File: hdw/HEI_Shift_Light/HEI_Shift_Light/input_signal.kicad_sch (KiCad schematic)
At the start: 14 parts

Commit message: more schematic progress
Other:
- note added: "Unsure on if this is supposed to be resistor to GND or midrail"
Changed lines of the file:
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@@
+		)
+	)
+	(bezier
+		(pts
+			(xy 124.46 77.47) (xy 124.46 77.47) (xy 104.14 49.53) (xy 104.14 49.53)
+		)
+		(stroke
+			(width 0)
+			(type default)
+		)
+		(fill
+			(type none)
 		)
 	)
@@
 		(exclude_from_sim no)
 		(at 199.136 62.992 0)
+		(effects
+			(font
+				(size 1.27 1.27)
+			)
+		)
+	)
+	(text "Unsure on if this is supposed to\nbe resistor to GND or midrail"
+		(exclude_from_sim no)
+		(at 103.378 47.752 0)
 		(effects
 			(font
@@
 			(hide yes)
 			(show_name no)
+			(do_not_autoplace no)
+			(effects
+				(font
+					(size 1.27 1.27)
+				)
+				(justify left)
+			)
+		)
+	)
+	(global_label "TACH_PULSE"
+		(shape output)
+		(at 157.48 40.64 0)
+		(fields_autoplaced yes)
+		(effects
+			(font
+				(size 1.27 1.27)
+			)
+			(justify left)
+		)
+		(property "Intersheetrefs" "${INTERSHEET_REFS}"
+			(at 172.0766 40.64 0)
+			(hide yes)
+			(show_name no)

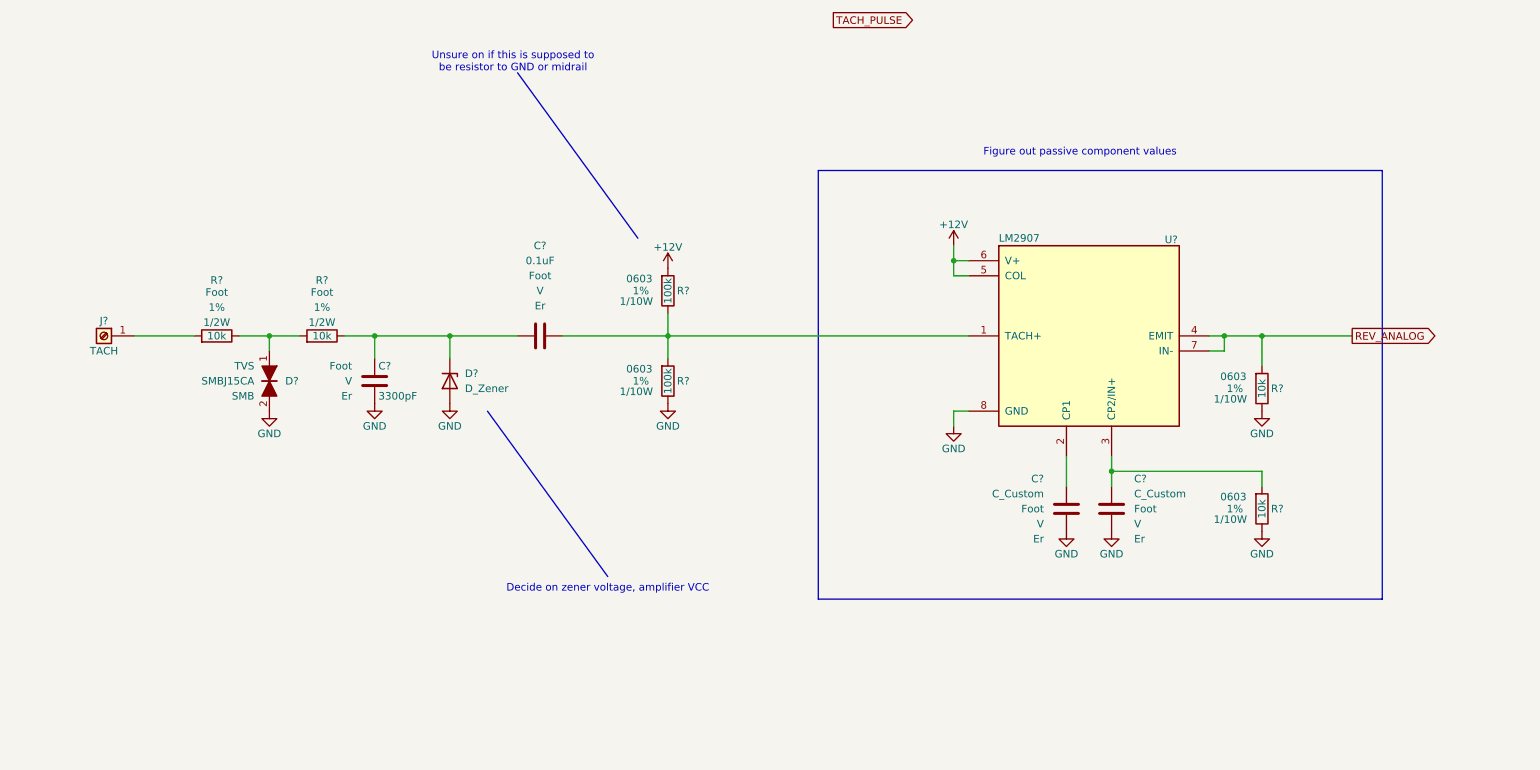
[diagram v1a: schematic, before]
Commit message: populated input protection circuit passive components, updated PIC pinout, added stuff to frequency to voltage converter circuit
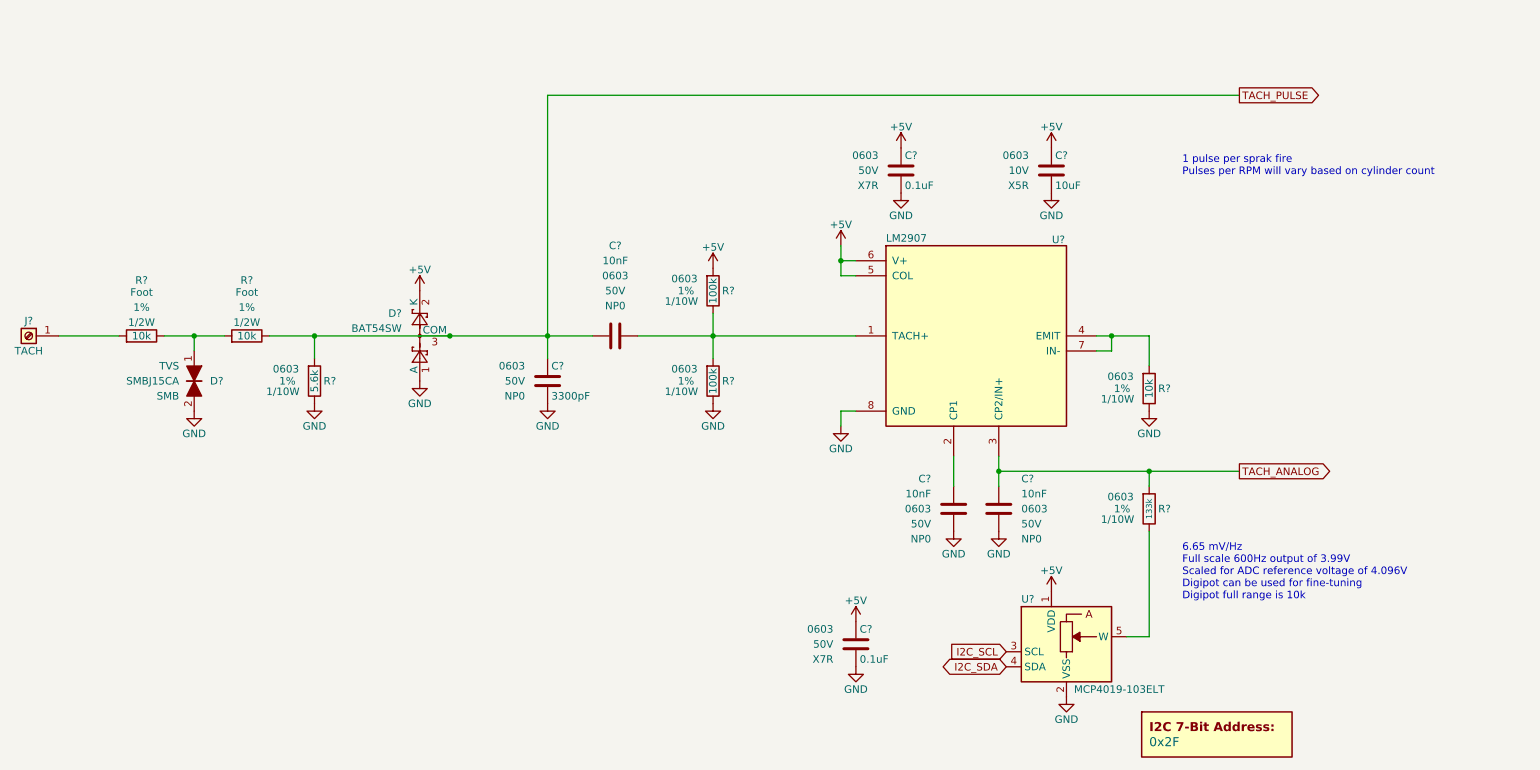
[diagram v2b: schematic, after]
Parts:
- removed C?: 0.1uF, symbol Custom Library:C_Custom
- removed C?: C_Custom, symbol Custom Library:C_Custom
- removed D?: D_Zener, symbol Device:D_Zener
- added C? (x2): 0.1uF, Capacitors_SMD:C_0603, symbol Custom_Library:C_Custom
- added C?: 10uF, Capacitors_SMD:C_0603, symbol Custom_Library:C_Custom
- added C? (x2): 10nF, symbol Custom Library:C_Custom
- added D?: BAT54SW, Package_TO_SOT_SMD:SOT-323_SC-70, symbol Diode:BAT54SW
- added DOC?: 0x2F, symbol Custom Library:I2C_Address
- added R?: 5.6k, Resistors_SMD:R_0603, symbol Custom_Library:R_Custom
- added U?: MCP4019-103ELT, Package_TO_SOT_SMD:SOT-353_SC-70-5, symbol Potentiometer_Digital:MCP4019-xxxxLT
- C?: Dielectric Er -> NP0; Voltage V -> 50V; display_footprint Foot -> 0603
- C?: value C_Custom -> 10nF; Dielectric Er -> NP0; Digi-Key PN PN -> 311-3960-1-ND; Voltage V -> 50V; display_footprint Foot -> 0603
- R?: value 10k -> 133k; Digi-Key PN 541-10.0KHCT-ND -> (none)
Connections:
- net GND: now also C?.2, C?.2, C?.2, C?.2, D?.1 (A), R?.2, U?.2 (VSS); no longer R?.2
- net TACH_PULSE: now also C?.1, R?.2, C?.1, D?.3 (COM), R?.1
- net TACH_ANALOG: now reaches R?.1, U?.3 (CP2/IN+)
- net TACH_ANALOG: now also C?.1
- net at R?.1, R?.2, U?.1 (TACH+): now also C?.2
- net +12V renamed +5V
- net +5V: now also C?.1, C?.1, C?.1, D?.2 (K), U?.1 (VDD)
- net REV_ANALOG: no longer names the net of R?.1, U?.4 (EMIT), U?.7 (IN-)
- new net: R?.2, U?.5 (W)
- new net I2C_SCL: U?.3 (SCL)
- new net I2C_SDA: U?.4 (SDA)
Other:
- note added: "1 pulse per sprak fire Pulses per RPM will vary based on cylinder count"
- note added: "6.65 mV/Hz Full scale 600Hz output of 3.99V Scaled for ADC reference voltage of 4.096V Digipot can be used for fine-tuning Digipot full range is 10k"
- note removed: "Decide on zener voltage, amplifier VCC"
- note removed: "Figure out passive component values"
- note removed: "Unsure on if this is supposed to be resistor to GND or midrail"
- moved on the sheet: C?, D?, J?, R?, U?

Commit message: added more shit, RGD LED, LC input filter
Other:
- note added: "1 pulse per spark fire Pulses per RPM will vary based on cylinder count"
- note removed: "1 pulse per sprak fire Pulses per RPM will vary based on cylinder count"
- company: (none) -> Drew Maatman
- title: (none) -> HEI Shift Light
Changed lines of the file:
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@@
 	(generator_version "10.0")
 	(paper "A")
+	(title_block
+		(title "HEI Shift Light")
+		(date "2026-05-29")
+		(rev "A")
+		(company "Drew Maatman")
+	)
 	(text "6.65 mV/Hz\nFull scale 600Hz output of 3.99V\nScaled for ADC reference voltage of 4.096V\nDigipot can be used for fine-tuning\nDigipot full range is 10k"
 		(exclude_from_sim no)
@@
 		)
 	)
-	(text "1 pulse per sprak fire\nPulses per RPM will vary based on cylinder count"
+	(text "1 pulse per spark fire\nPulses per RPM will vary based on cylinder count"
 		(exclude_from_sim no)
 		(at 216.408 65.278 0)
@@
 		(in_pos_files yes)
 		(dnp no)
-		(property "Reference" "#PWR044"
+		(property "Reference" "#PWR?"
 			(at 168.91 76.2 0)
 			(hide yes)
@@
 			(project "HEI_Shift_Light"
 				(path "/288c8230-69eb-4ad9-929d-f4630114196f/3f3e3aac-043b-4713-af21-26e9e85000ef"
-					(reference "#PWR044")
+					(reference "#PWR?")
 					(unit 1)
 				)
@@
 		(in_pos_files yes)
 		(dnp no)
-		(property "Reference" "#PWR03"
+		(property "Reference" "#PWR?"
 			(at 87.63 107.95 0)
 			(hide yes)
@@
 			(project "HEI_Shift_Light"
 				(path "/288c8230-69eb-4ad9-929d-f4630114196f/3f3e3aac-043b-4713-af21-26e9e85000ef"
-					(reference "#PWR03")
+					(reference "#PWR?")
 					(unit 1)
 				)
@@
 		(in_pos_files yes)
 		(dnp no)
-		(property "Reference" "#PWR05"
+		(property "Reference" "#PWR?"
 			(at 194.31 140.97 0)
 			(hide yes)
@@
 			(project "HEI_Shift_Light"
 				(path "/288c8230-69eb-4ad9-929d-f4630114196f/3f3e3aac-043b-4713-af21-26e9e85000ef"
-					(reference "#PWR05")
+					(reference "#PWR?")
 					(unit 1)
 				)
@@
 		(in_pos_files yes)
 		(dnp no)
-		(property "Reference" "#PWR01"
+		(property "Reference" "#PWR?"
 			(at 158.75 82.55 0)
 			(hide yes)
@@
 			(project "HEI_Shift_Light"
 				(path "/288c8230-69eb-4ad9-929d-f4630114196f/3f3e3aac-043b-4713-af21-26e9e85000ef"
-					(reference "#PWR01")
+					(reference "#PWR?")
 					(unit 1)
 				)
@@
 		(in_pos_files yes)
 		(dnp no)
-		(property "Reference" "#PWR038"
+		(property "Reference" "#PWR?"
 			(at 196.85 161.29 0)
 			(hide yes)
@@
 			(project "HEI_Shift_Light"
 				(path "/288c8230-69eb-4ad9-929d-f4630114196f/3f3e3aac-043b-4713-af21-26e9e85000ef"
-					(reference "#PWR038")
+					(reference "#PWR?")
 					(unit 1)
 				)
@@
 		(in_pos_files yes)
 		(dnp no)
-		(property "Reference" "#PWR039"
+		(property "Reference" "#PWR?"
 			(at 69.85 111.76 0)
 			(hide yes)
@@
 			(project "HEI_Shift_Light"
 				(path "/288c8230-69eb-4ad9-929d-f4630114196f/3f3e3aac-043b-4713-af21-26e9e85000ef"
-					(reference "#PWR039")
+					(reference "#PWR?")
 					(unit 1)
 				)
@@
 		(in_pos_files yes)
 		(dnp no)
-		(property "Reference" "#PWR037"
+		(property "Reference" "#PWR?"
 			(at 137.16 86.36 0)
 			(hide yes)
@@
 			(project "HEI_Shift_Light"
 				(path "/288c8230-69eb-4ad9-929d-f4630114196f/3f3e3aac-043b-4713-af21-26e9e85000ef"
-					(reference "#PWR037")
+					(reference "#PWR?")
 					(unit 1)
 				)
@@
 		(in_pos_files yes)
 		(dnp no)
-		(property "Reference" "#PWR043"
+		(property "Reference" "#PWR?"
 			(at 168.91 66.04 0)
 			(hide yes)
@@
 			(project "HEI_Shift_Light"
 				(path "/288c8230-69eb-4ad9-929d-f4630114196f/3f3e3aac-043b-4713-af21-26e9e85000ef"
-					(reference "#PWR043")
+					(reference "#PWR?")
 					(unit 1)
 				)
@@
 		(in_pos_files yes)
 		(dnp no)
-		(property "Reference" "#PWR048"
+		(property "Reference" "#PWR?"
 			(at 161.29 156.21 0)
 			(hide yes)
@@
 			(project "HEI_Shift_Light"
 				(path "/288c8230-69eb-4ad9-929d-f4630114196f/3f3e3aac-043b-4713-af21-26e9e85000ef"
-					(reference "#PWR048")
+					(reference "#PWR?")
 					(unit 1)
 				)
@@
 		(in_pos_files yes)
 		(dnp no)
-		(property "Reference" "#PWR040"
+		(property "Reference" "#PWR?"
 			(at 87.63 90.17 0)
 			(hide yes)
@@
 			(project "HEI_Shift_Light"
 				(path "/288c8230-69eb-4ad9-929d-f4630114196f/3f3e3aac-043b-4713-af21-26e9e85000ef"
-					(reference "#PWR040")
+					(reference "#PWR?")
 					(unit 1)
 				)
@@
 		(in_pos_files yes)
 		(dnp no)
-		(property "Reference" "#PWR06"
+		(property "Reference" "#PWR?"
 			(at 137.16 111.76 0)
 			(hide yes)
@@
 			(project "HEI_Shift_Light"
 				(path "/288c8230-69eb-4ad9-929d-f4630114196f/3f3e3aac-043b-4713-af21-26e9e85000ef"
-					(reference "#PWR06")
+					(reference "#PWR?")
 					(unit 1)
 				)
@@
 		(in_pos_files yes)
 		(dnp no)
-		(property "Reference" "#PWR047"
+		(property "Reference" "#PWR?"
 			(at 161.29 146.05 0)
 			(hide yes)
@@
 			(project "HEI_Shift_Light"
 				(path "/288c8230-69eb-4ad9-929d-f4630114196f/3f3e3aac-043b-4713-af21-26e9e85000ef"
-					(reference "#PWR047")
+					(reference "#PWR?")
 					(unit 1)
 				)
@@
 		(in_pos_files yes)
 		(dnp no)
-		(property "Reference" "#PWR04"
+		(property "Reference" "#PWR?"
 			(at 109.22 111.76 0)
 			(hide yes)
@@
 			(project "HEI_Shift_Light"
 				(path "/288c8230-69eb-4ad9-929d-f4630114196f/3f3e3aac-043b-4713-af21-26e9e85000ef"
-					(reference "#PWR04")
+					(reference "#PWR?")
 					(unit 1)
 				)
@@
 		(in_pos_files yes)
 		(dnp no)
-		(property "Reference" "#PWR02"
+		(property "Reference" "#PWR?"
 			(at 49.53 113.03 0)
 			(hide yes)
@@
 			(project "HEI_Shift_Light"
 				(path "/288c8230-69eb-4ad9-929d-f4630114196f/3f3e3aac-043b-4713-af21-26e9e85000ef"
-					(reference "#PWR02")
+					(reference "#PWR?")
 					(unit 1)
 				)
@@
 		(in_pos_files yes)
 		(dnp no)
-		(property "Reference" "#PWR045"
+		(property "Reference" "#PWR?"
 			(at 194.31 66.04 0)
 			(hide yes)
@@
 			(project "HEI_Shift_Light"
 				(path "/288c8230-69eb-4ad9-929d-f4630114196f/3f3e3aac-043b-4713-af21-26e9e85000ef"
-					(reference "#PWR045")
+					(reference "#PWR?")
 					(unit 1)
 				)
@@
 		(in_pos_files yes)
 		(dnp no)
-		(property "Reference" "#PWR046"
+		(property "Reference" "#PWR?"
 			(at 194.31 76.2 0)
 			(hide yes)
@@
 			(project "HEI_Shift_Light"
 				(path "/288c8230-69eb-4ad9-929d-f4630114196f/3f3e3aac-043b-4713-af21-26e9e85000ef"
-					(reference "#PWR046")
+					(reference "#PWR?")
 					(unit 1)
 				)
